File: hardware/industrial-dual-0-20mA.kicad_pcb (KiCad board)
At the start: 2 copper layers, 40 x 40 mm, 32 parts, among them P1 CON-SENSOR, P2 P-PWR-8GN, Q1 FDN5630, U1 M24C64, U2 NC7WB66K8X, U3 MCP3423, U4 DRILL, U5 DRILL, U6 DRILL, U7 DRILL

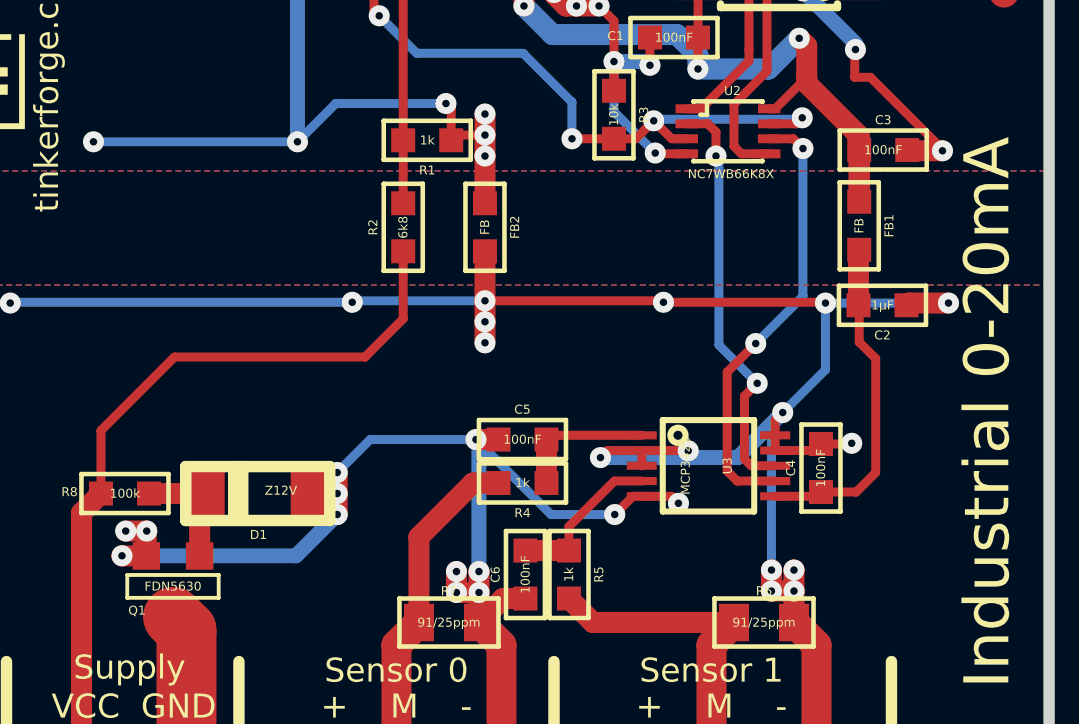
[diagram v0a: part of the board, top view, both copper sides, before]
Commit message: set mcp3423 pin ADR1 to floating
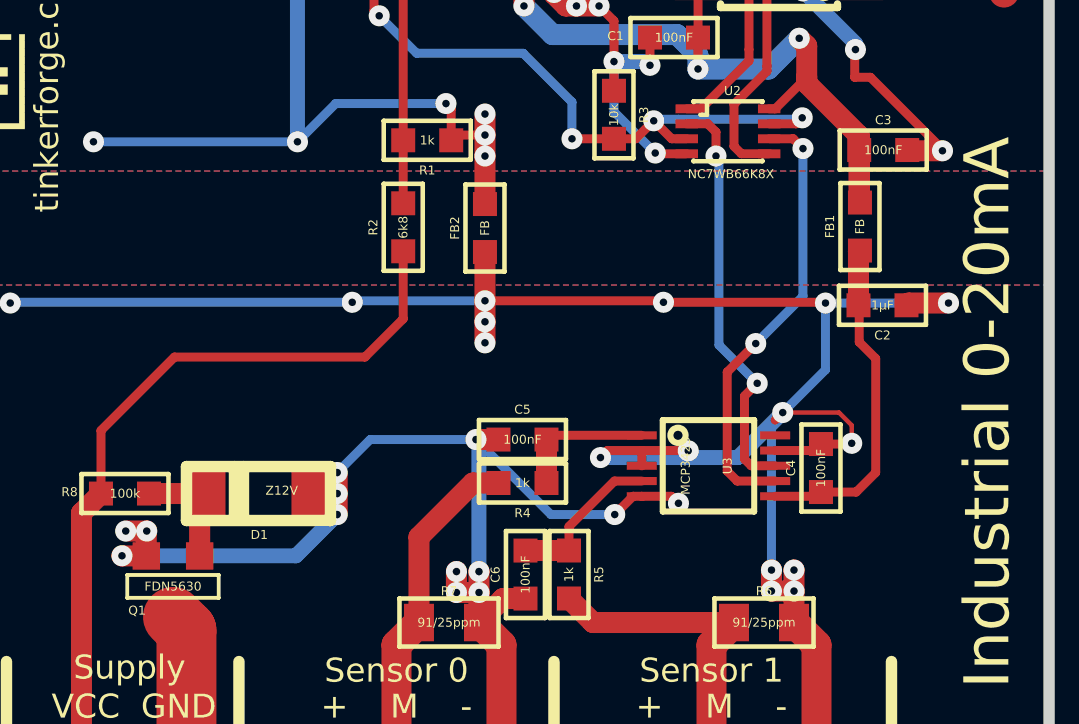
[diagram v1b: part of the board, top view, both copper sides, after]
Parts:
- turned FB1 to 90 degrees
- turned FB2 to 90 degrees
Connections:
- FB1 pad 1: 3V3 -> +3.3VP
- FB1 pad 2: +3.3VP -> 3V3
- FB2 pad 1: GND -> AGND
- FB2 pad 2: AGND -> GND
- U3 pad 10: AGND -> (no net)
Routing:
- net AGND: track 109.4 -> 111.5 mm

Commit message: Add 3d information (final)
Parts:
- C1, C2, C3, C4, C5, C6, FB1, FB2: footprint 0603 -> C0603
- Fiducial_Mark (x2): footprint Fiducial_Mark -> kicad-libraries:Fiducial_Mark
- G***: footprint Logo_31x31 -> kicad-libraries:Logo_31x31
- R1, R2, R3, R4, R5, R8: footprint 0603 -> R0603
- R6, R7: footprint 0805 -> R0805
- VAL: footprint CE_5mm -> kicad-libraries:CE_5mm
- VAL: footprint WEEE_7mm -> kicad-libraries:WEEE_7mm
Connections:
- P1 pad 1: (no net) -> Net-(P1-Pad1)
- P1 pad 10: (no net) -> Net-(P1-Pad10)
- P1 pad 9: (no net) -> Net-(P1-Pad9)
- U1 pad 7: (no net) -> Net-(U1-Pad7)
- U3 pad 10: (no net) -> Net-(U3-Pad10)
